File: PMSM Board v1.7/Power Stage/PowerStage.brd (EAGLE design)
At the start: 102.5 x 79.9 mm, 20 parts, among them U1 TPS73733-Q1_DRB_8, U2 TPS54240_DRC_10, U3 LP38692_NGG_6

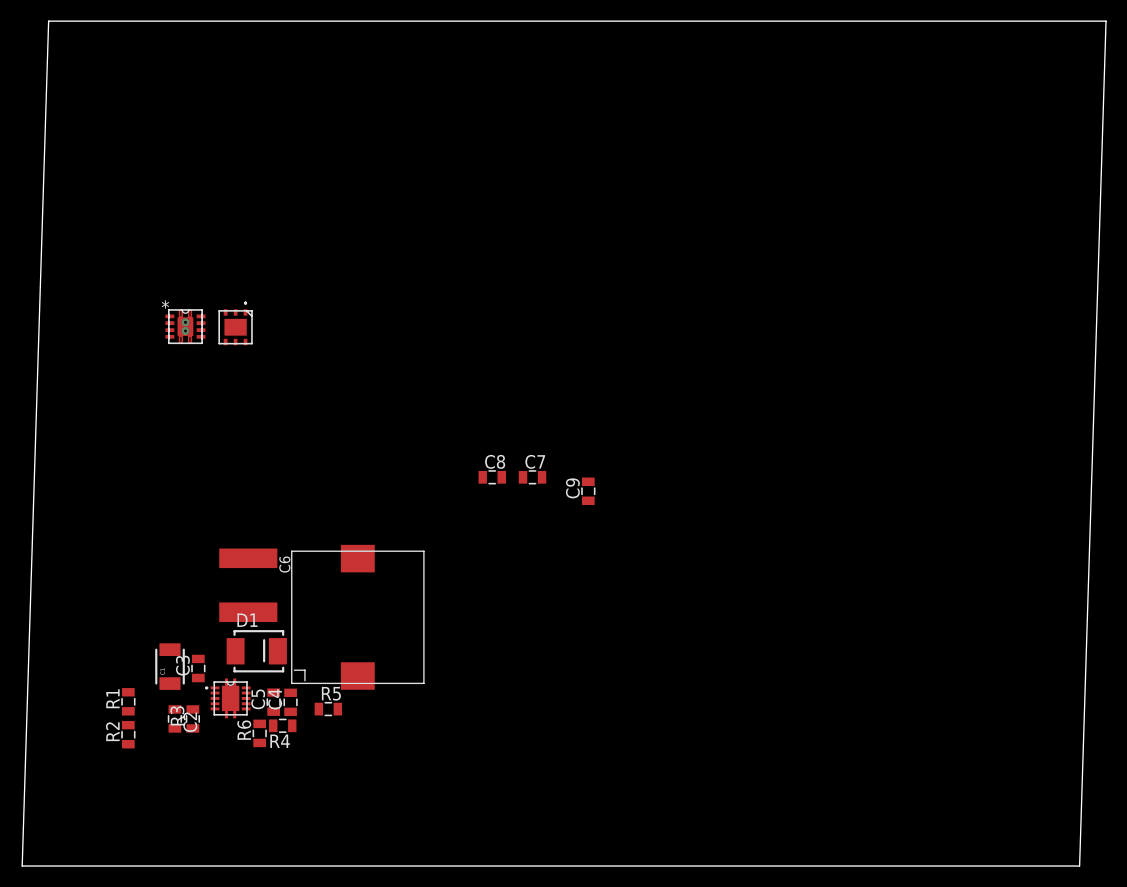
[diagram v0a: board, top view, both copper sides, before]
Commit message: rerouting PMSM Board
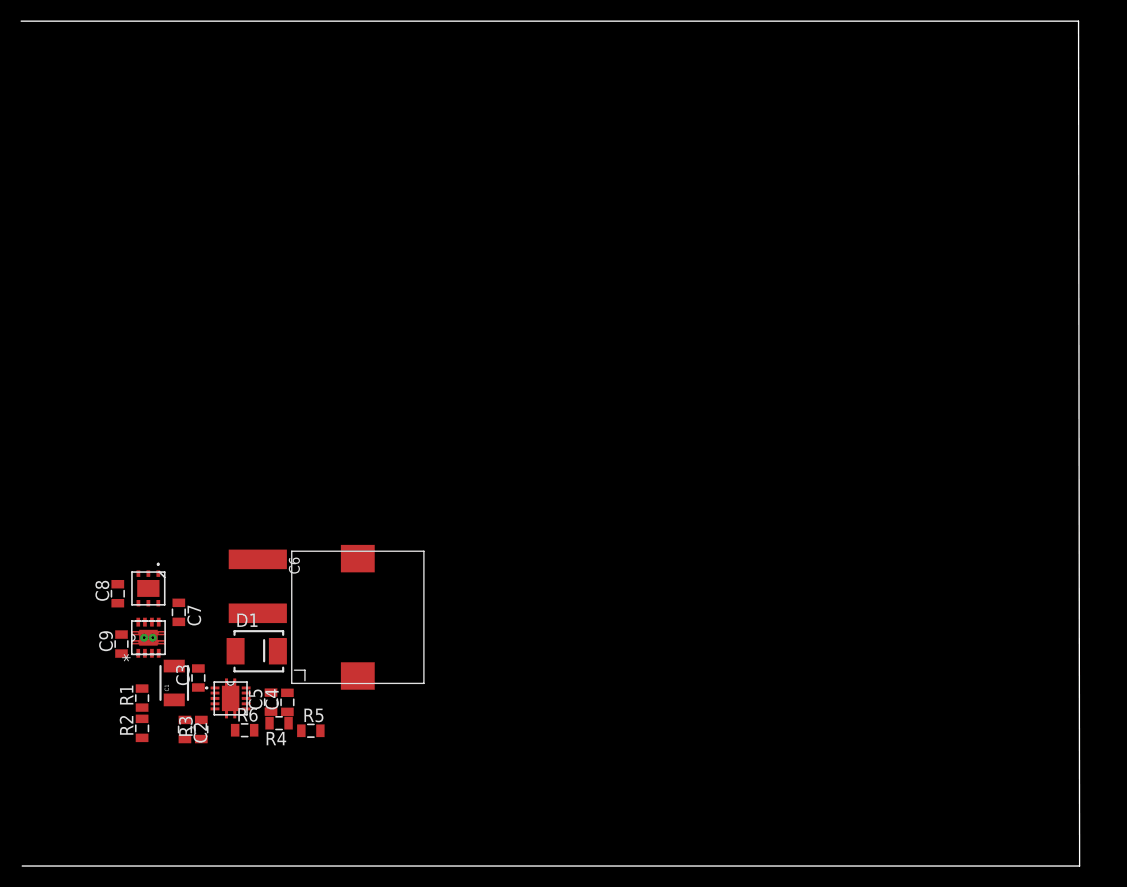
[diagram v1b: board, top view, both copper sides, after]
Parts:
- moved C9 46.5 mm to (6.89, 21.1)
- moved C8 37.1 mm to (6.54, 25.9), turned to 90 degrees
- moved C7 35.8 mm to (12.3, 24.1), turned to 270 degrees
- moved U1 29.6 mm to (9.44, 21.7), turned to 90 degrees
- moved U3 26.0 mm to (9.43, 26.4)
- moved R5 2.63 mm to (24.8, 12.9)
- moved C1 1.60 mm to (11.9, 17.4)
- moved R6 1.45 mm to (18.5, 12.9), turned to 0 degrees
- moved R2 1.43 mm to (8.84, 13.1)
- moved C2 1.38 mm to (12.9, 13.0)
- moved R1 1.35 mm to (8.84, 16.0)
- moved R3 1.28 mm to (14.4, 13.0)
- moved C6 0.91 mm to (19.8, 26.6)
- moved C3 0.90 mm to (14.2, 17.9)
- moved R4 0.43 mm to (21.8, 13.6)
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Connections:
- net GND: now also U3.7
- net VCC5V0: now also C8.1
- net VCC5V5: now also C7.1
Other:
- board size 102.5 x 79.9 mm -> 100.1 x 79.9 mm
